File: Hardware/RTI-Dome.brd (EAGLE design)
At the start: 119.4 x 71.2 mm, 86 parts, among them IC1 24AA128ST, IC3 FT232RL, IC4 REG1117, IC5 74LVC245, IC6 74ABT245, J1 POWERPOLE_POWER45A, U1 W5500, X13 PN61729-S, X9 J1011F21PNL

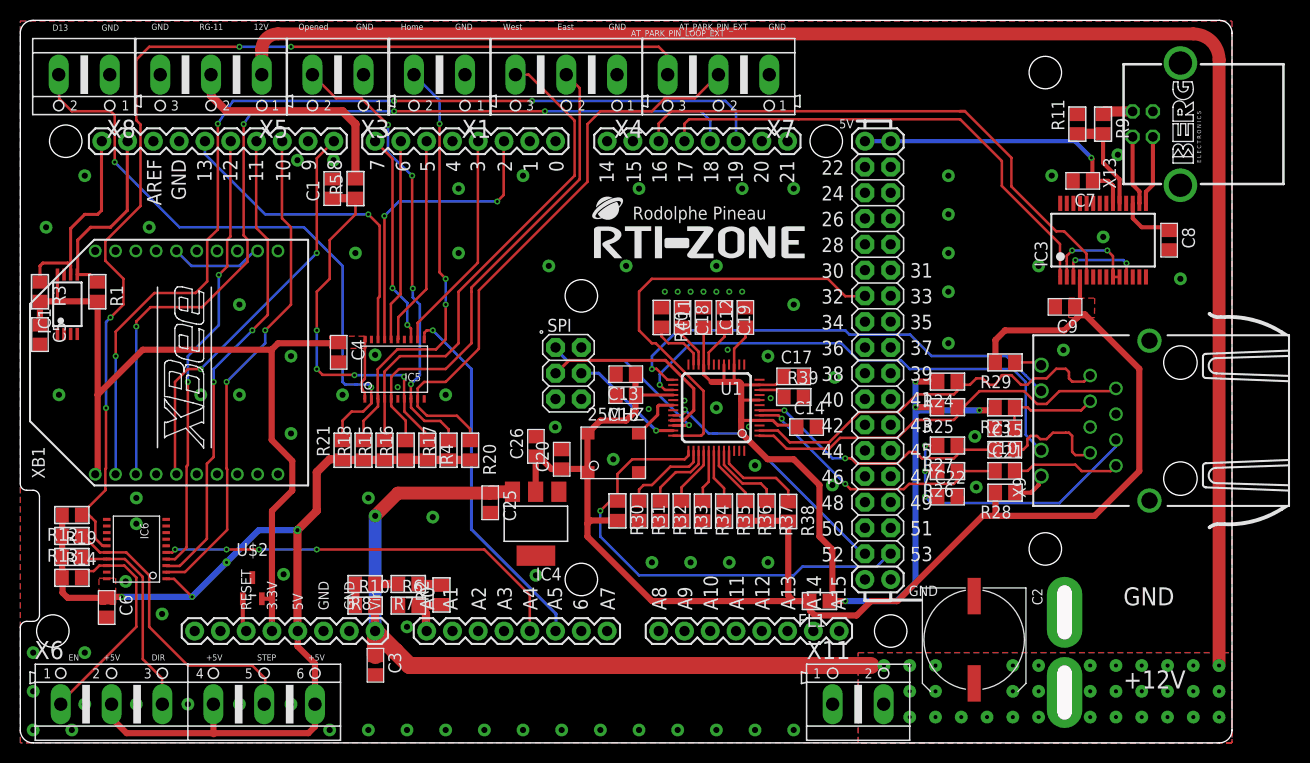
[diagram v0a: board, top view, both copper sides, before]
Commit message: Revert "Cleanup unused boards and sketches"
This reverts commit 55a3d73229767f07f24b7c99b357f5ead4999c3a.
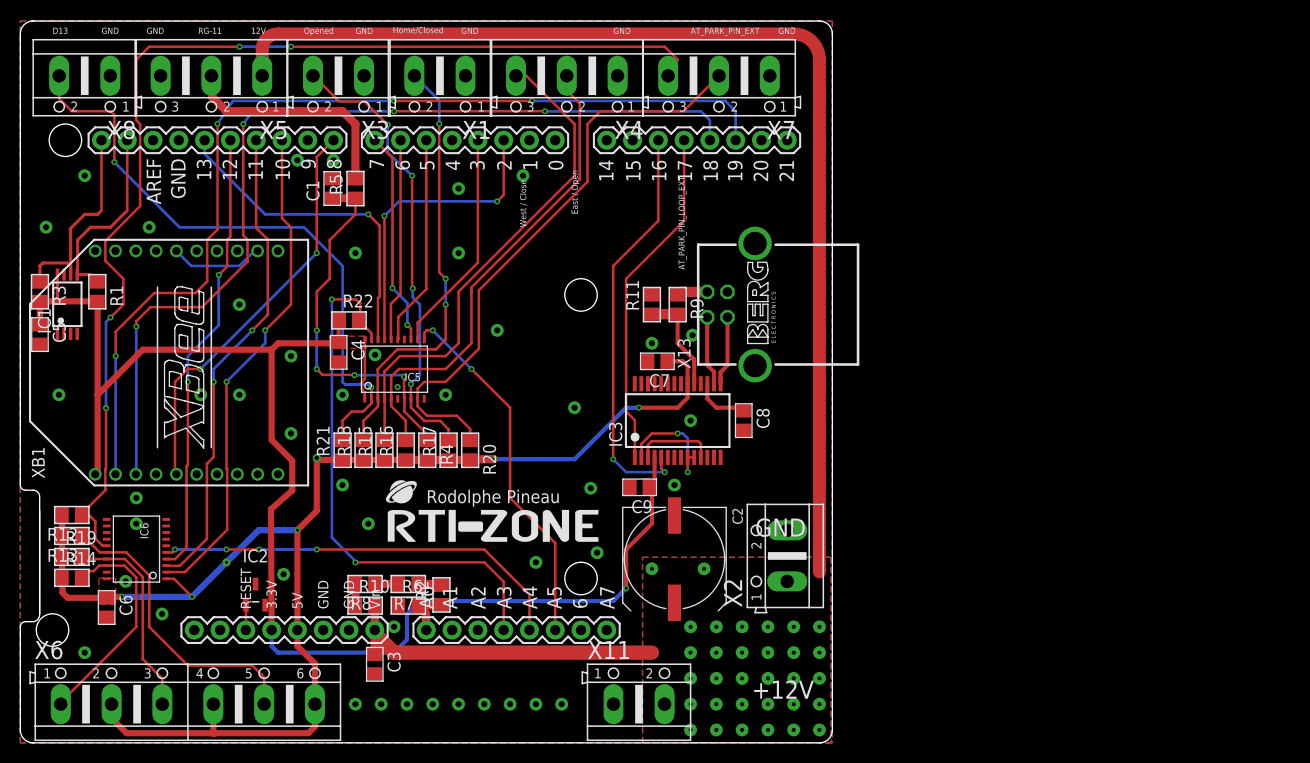
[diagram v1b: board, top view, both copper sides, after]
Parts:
- removed 25MHZ: CB3LV-OSCILATOR, rti:CB3
- removed C10: 22nF, rti:C0805
- removed C11, C12, C14, C16, C17, C20: 100nF, rti:C0805
- removed C13, C18, C22: 10nF, rti:C0805
- removed C15, C21: 6.8nF, rti:C0805
- removed C19: 4.7uF, rti:C0805
- removed C25, C26: 10uF, rti:C0805
- removed FL1: BLM21AG121SN1D, BLM21AG121SN1D:L0805
- removed IC4: REG1117, burr-brown:SOT223
- removed J1: POWERPOLE_POWER45A, powerpoles:POWERPOLE_PAIR_45A
- removed R23: 10 1%, rti:R0805
- removed R24, R25, R26, R27: 49.9 1%, rti:R0805
- removed R28, R29: 330, rti:R0805
- removed R30, R31, R32, R33, R34, R35, R36, R37, R38, R40: 4.7K, rti:R0805
- removed R39: 12.4K 1%, rti:R0805
- removed U$1: ARDUINO_DUE_SHIELD_FULL, arduino_shield:ARDUINO_DUE_SHIELD_FULL
- removed U$2: MCP120T-270I_TT, MCP120T-270I_TT:SOT95P237X112-3N
- removed U1: W5500, W5500:LQFP48
- removed X9: J1011F21PNL, rti:J1
- added IC2: MCP120T-270I_TT, MCP120T-270I_TT:SOT95P237X112-3N
- added PCB1: ARDUINO_DUE_SHIELD_SHORT, arduino_shield:ARDUINO_DUE_SHIELD_SHORT
- added R22: 4.7K, rti:R0805
- added X2: (no value), con-ptr500:AK500/2
- moved IC3 45.5 mm to (64.8, 31.8)
- moved R9 45.5 mm to (64.8, 43.2)
- moved R11 45.5 mm to (62.2, 43.2)
- moved C7 45.5 mm to (62.8, 37.6)
- moved C8 45.5 mm to (71.3, 31.8)
- moved C9 45.5 mm to (61.0, 25.2)
- moved X13 45.5 mm to (72.4, 43.2)
- moved U$4 34.5 mm to (36.2, 19.8)
- moved C2 30.6 mm to (64.5, 18.1)
- moved X11 21.6 mm to (61.0, 3.81)
- moved X7 0.13 mm to (68.8, 65.7)
- moved X3 0.12 mm to (31.4, 65.7)
- moved X1 0.12 mm to (41.4, 65.7)
- moved X4 0.12 mm to (53.8, 65.7)
- moved X8 0.12 mm to (6.35, 65.7)
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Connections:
- removed net +3V3: 25MHZ.1, 25MHZ.4, C13.1, C16.1, C20.1, C26.1, C9.1, FL1.2, IC3.4, IC4.2, R28.2, R29.2, R30.2, R36.2, R37.2, R38.2, U1.28
- removed net +5V: U$1.+5V_
- removed net ACT_LED: U1.27, X9.11
- removed net AVDD: C11.1, C12.1, C14.1, C17.1, FL1.1, R23.2, R24.2, R25.2, U1.11, U1.15, U1.17, U1.21, U1.4, U1.8
- removed net ETH_CS: U$1.52, U1.32
- removed net ETH_RESET: R30.1, U$1.53, U1.37
- removed net INT_N: U$1.32, U1.36
- removed net LINK_ACK: U1.25, X9.10
- removed net N$10: R28.1, X9.12
- removed net N$11: C15.2, X9.7
- removed net N$12: C21.2, X9.8
- removed net N$13: C10.1, R23.1, X9.3
- removed net N$17: U1.26
- removed net N$22: R31.1, U1.38
- removed net N$23: R32.1, U1.39
- removed net N$24: R33.1, U1.40
- removed net N$25: R34.1, U1.41
- removed net N$26: R35.1, U1.42
- removed net N$27: R36.1, U1.43
- removed net N$28: R37.1, U1.44
- removed net N$29: R38.1, U1.45
- removed net N$31: C19.2, U1.20
- removed net N$32: U1.18
- removed net N$33: C18.2, U1.22
- removed net N$34: R39.1, U1.10
- removed net N$35: R40.2, U1.23
- removed net N$7: C22.1, R26.2, R27.2, X9.6
- removed net N$8: R29.1, X9.9
- removed net RXN: C21.1, R26.1, U1.5
- removed net RXP: C15.1, R27.1, U1.6
- removed net SCLK: U$1.SCK, U1.33
- removed net SDI: U$1.MISO, U1.34
- removed net SDO: U$1.MOSI, U1.35
- removed net TXN: R25.1, U1.1, X9.2
- removed net TXP: R24.1, U1.2, X9.1
- removed net XI: 25MHZ.3, U1.30
- removed net XO: U1.31
- new net BUF_EN: IC5.P$19, PCB1.A3, R22.2
- net +12V: now also PCB1.VIN, X2.1; no longer C25.1, IC4.3, J1.RED, U$1.VIN
- net 3.3V: now also C9.1, IC2.2, IC3.4, PCB1.3.3V, R22.1; no longer U$1.3.3V, U$2.2
- net AT_PARK_PIN: now also PCB1.A5; no longer U$1.A5
- net AT_PARK_PIN_LOOP: now also PCB1.A4; no longer U$1.A4
- net BUTTON_EAST_OPEN: now also PCB1.5; no longer U$1.5
- net BUTTON_WEST_CLOSE: now also PCB1.6; no longer U$1.6
- net D13: now also PCB1.13; no longer U$1.13
- net GND: now also IC2.3, PCB1.GND, PCB1.GND., PCB1.GND.., X2.2; no longer 25MHZ.2, C10.2, C11.2, C12.2, C13.2, C14.2, C16.2, C17.2, C18.1, C19.1, C20.2, C22.2, C25.2, C26.2, IC4.1, IC5.P$19, J1.BLACK, R31.2, R32.2, R33.2, R34.2, R35.2, R39.2, R40.1, U$1.GND, U$1.GND., U$1.GND.., U$1.GND..., U$1.GND...., U$1.GND__, U$2.3, U1.14, U1.16, U1.19, U1.29, U1.3, U1.48, U1.9, X9.4, X9.5, X9.M1, X9.M2
- net HOME_SHUTTER_CLOSED: now also PCB1.2; no longer U$1.2
- net M_DIR: now also PCB1.11; no longer U$1.11
- net M_EN: now also PCB1.10; no longer U$1.10
- net M_STEP: now also PCB1.12; no longer U$1.12
- net RESET: now also IC2.1, PCB1.RESET; no longer U$1.RESET, U$2.1
- net RG-11: now also PCB1.7; no longer U$1.7
- net RX2: now also PCB1.17; no longer U$1.17
- net SCL: now also PCB1.SCL1; no longer U$1.SCL1
- net SDA: now also PCB1.SDA1; no longer U$1.SDA1
- net SHUTTER_OPENED: now also PCB1.3; no longer U$1.3
- net TX2: now also PCB1.16; no longer U$1.16
- net VCC: now also PCB1.5V; no longer U$1.5V, U$1.5V., U$1.5V..
- net VPIN: now also PCB1.A0; no longer U$1.A0
- net XBEE_DIN: now also PCB1.18; no longer U$1.18
- net XBEE_DOUT: now also PCB1.19; no longer U$1.19
- net XBEE_RESET: now also PCB1.8; no longer U$1.8
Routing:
- net +3V3: track 146.7 -> 0.00 mm
- net AVDD: track 96.8 -> 0.00 mm, vias 4 -> 0
- net +12V: track 239.2 -> 143.0 mm, vias 34 -> 32
- net 3.3V: track 90.3 -> 147.0 mm, vias 0 -> 1
- net BUF_EN: track 0.00 -> 54.1 mm, vias 0 -> 2
- net ACT_LED: track 48.9 -> 0.00 mm, vias 1 -> 0
- net ETH_RESET: track 46.6 -> 0.00 mm, vias 1 -> 0
- net LINK_ACK: track 45.7 -> 0.00 mm, vias 1 -> 0
- net INT_N: track 43.4 -> 0.00 mm
- net TXN: track 39.7 -> 0.00 mm
- net TXP: track 39.4 -> 0.00 mm
- net N$7: track 30.8 -> 0.00 mm, vias 3 -> 0
- net RXN: track 27.6 -> 0.00 mm, vias 2 -> 0
- net RXP: track 27.4 -> 0.00 mm, vias 2 -> 0
- net ETH_CS: track 25.5 -> 0.00 mm, vias 1 -> 0
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- removed copper zone on layer 1, net +3V3
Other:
- board size 119.4 x 71.2 mm -> 80 x 71.1 mm
- board text added: "East / Open"
- board text added: "Home/Closed"
- board text added: "West / Close"
- board text removed: "+5V"
- board text removed: "DIR"
- board text removed: "Dome Rotator"
- board text removed: "EN"
- board text removed: "East"
- board text removed: "Home"
- board text removed: "STEP"
- board text removed: "West"
